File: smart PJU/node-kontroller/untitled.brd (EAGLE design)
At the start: 80 x 80 mm, 48 parts, among them J1 U.FL-R-SMT(01), J2 10118193-0001LF, K1 351, Q1 S9013, Q16 MMBT3904, Q17 MMBT3904, Q18 12MHz, U1 AMS1117, U19 CH340G, U2 PC817X2NIP0F

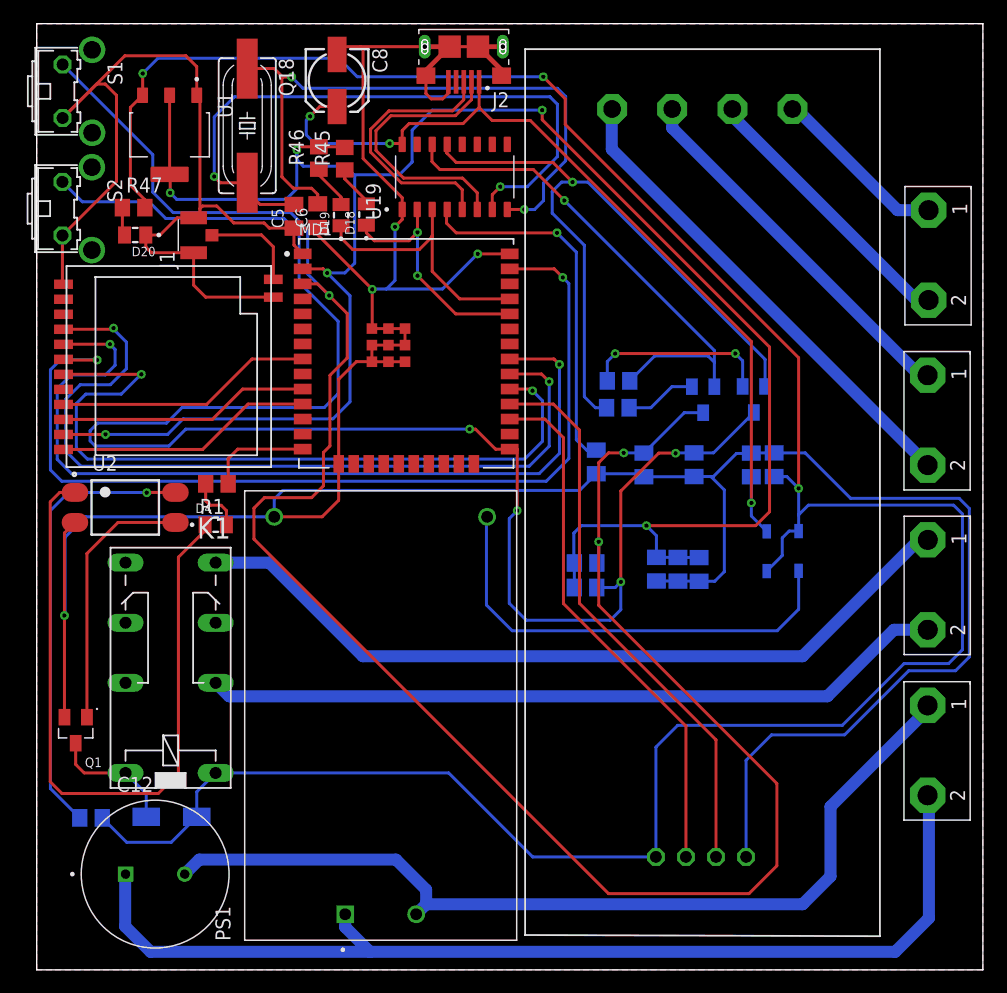
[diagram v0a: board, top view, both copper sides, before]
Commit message: revisi relay node dan list komponen
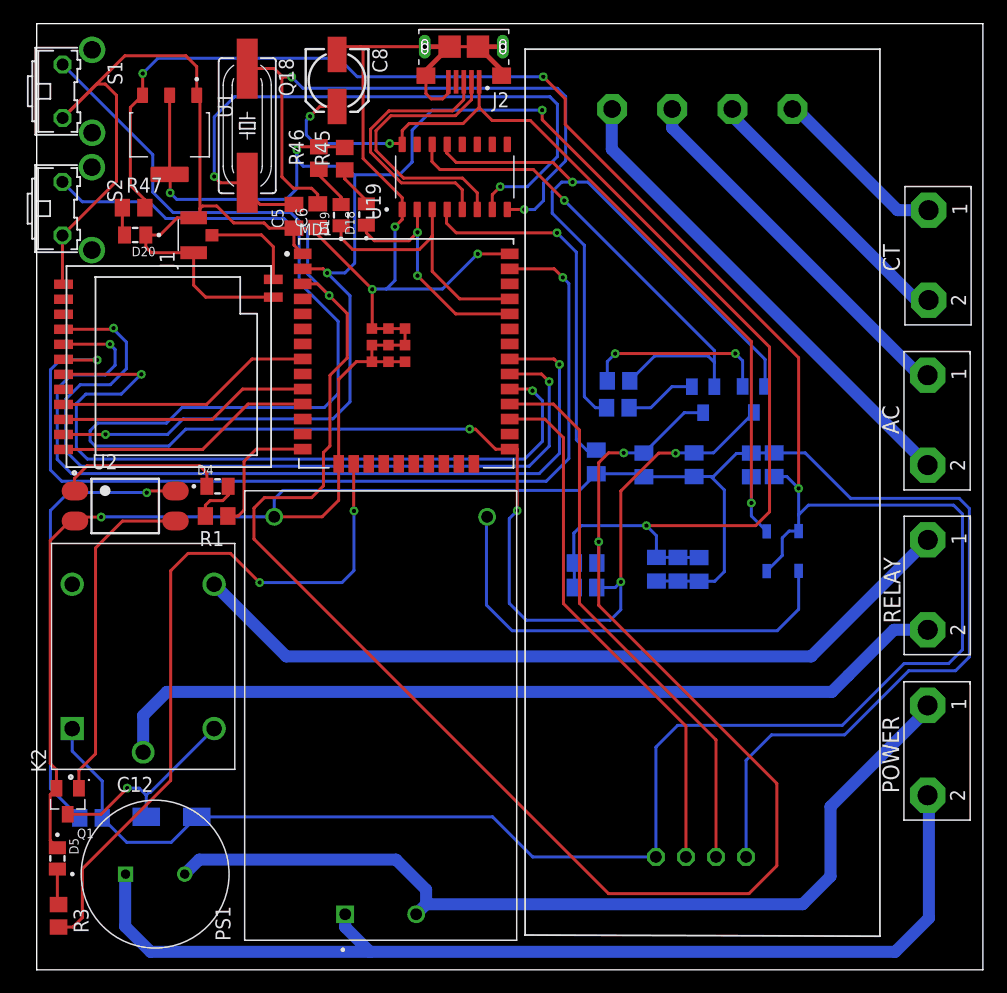
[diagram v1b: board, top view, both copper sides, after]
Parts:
- removed K1: 351, relay:351
- added D5: SML-LXT0805IW-TR, SML-LXT0805IW-TR:LEDC2012X120N
- added K2: SRD-05VDC-SL-C, SRD-05VDC-SL-C:RELAY_SRD-05VDC-SL-C
- added R3: 10k, rcl:R0805
- moved Q1 6.05 mm to (2.62, 14.3)
- moved D4 3.25 mm to (15.3, 40.9)
- moved R1 2.72 mm to (15.2, 38.4)
- moved U2 0.12 mm to (7.49, 39.2)
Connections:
- new net LED-LORA: MD1.16, R3.2
- new net N$12: D5.A, R3.1
- net GND: now also D5.C
- net N$10: now also K2.NO; no longer K1.S1
- net N$7: now also K2.A2; no longer K1.16
- net N$9: now also K2.COM; no longer K1.P1
- net VCC: now also K2.A1; no longer K1.1
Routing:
- net LED-LORA: track 0.00 -> 61.3 mm, vias 0 -> 2
- net N$4: track 60.0 -> 14.1 mm
- net N$9: track 63.0 -> 72.4 mm
- net N$7: track 10.8 -> 17.7 mm, vias 0 -> 1
- net N$6: track 22.4 -> 28.6 mm
- net GND: track 350.9 -> 355.4 mm
- net VCC: track 221.0 -> 225.3 mm
- net N$12: track 0.00 -> 3.04 mm
- net RELAY: track 8.77 -> 11.1 mm
- net N$8: track 4.72 -> 3.94 mm
- net N$10: track 67.6 -> 66.9 mm
- removed copper zone on layer 16, net N$12
- removed copper zone on layer 1, net N$13
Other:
- board text added: "AC"
- board text added: "CT"
- board text added: "POWER"
- board text added: "RELAY"

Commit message: revisi rangkaian
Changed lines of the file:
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@@
 <setting verticaltext="up"/>
 </settings>
-<grid distance="0.003125" unitdist="mic" unit="mm" style="lines" multiple="1" display="yes" altdistance="5" altunitdist="mil" altunit="mil"/>
+<grid distance="0.5" unitdist="mm" unit="mm" style="lines" multiple="1" display="yes" altdistance="5" altunitdist="mil" altunit="mil"/>
 <layers>
 <layer number="1" name="Top" color="4" fill="1" visible="yes" active="yes"/>
@@
 <wire x1="73.338565625" y1="25.897153125" x2="77.102621875" y2="25.897153125" width="0.254" layer="16"/>
 <wire x1="77.102621875" y1="25.897153125" x2="78.27220625" y2="27.0667375" width="0.254" layer="16"/>
-<wire x1="78.27220625" y1="27.0667375" x2="78.27220625" y2="38.539134375" width="0.254" layer="16"/>
-<wire x1="78.27220625" y1="38.539134375" x2="77.521609375" y2="39.28973125" width="0.254" layer="16"/>
-<wire x1="77.521609375" y1="39.28973125" x2="65.242903125" y2="39.28973125" width="0.254" layer="16"/>
-<wire x1="65.242903125" y1="39.28973125" x2="64.421646875" y2="38.468475" width="0.254" layer="16"/>
+<wire x1="78.27220625" y1="27.0667375" x2="78.27220625" y2="38.0002375" width="0.254" layer="16"/>
+<wire x1="78.27220625" y1="38.0002375" x2="77.113796875" y2="39.158646875" width="0.254" layer="16"/>
+<wire x1="77.113796875" y1="39.158646875" x2="65.11181875" y2="39.158646875" width="0.254" layer="16"/>
+<wire x1="65.11181875" y1="39.158646875" x2="64.421646875" y2="38.468475" width="0.254" layer="16"/>
 <wire x1="5.541034375" y1="12.848734375" x2="7.60865625" y2="10.7811125" width="0.254" layer="16"/>
 <wire x1="11.3760625" y1="10.7811125" x2="13.53185625" y2="12.93690625" width="0.254" layer="16"/>
@@
 <wire x1="77.686790625" y1="25.287809375" x2="78.857" y2="26.45801875" width="0.254" layer="16"/>
 <wire x1="78.857" y1="26.45801875" x2="78.857" y2="39.002490625" width="0.254" layer="16"/>
-<wire x1="78.857" y1="39.002490625" x2="77.99658125" y2="39.862909375" width="0.254" layer="16"/>
-<wire x1="77.99658125" y1="39.862909375" x2="68.821690625" y2="39.862909375" width="0.254" layer="16"/>
+<wire x1="78.857" y1="39.002490625" x2="77.83636875" y2="40.023121875" width="0.254" layer="16"/>
+<wire x1="77.83636875" y1="40.023121875" x2="68.661478125" y2="40.023121875" width="0.254" layer="16"/>
 <wire x1="64.979278125" y1="43.705321875" x2="62.35489375" y2="43.705321875" width="0.254" layer="16"/>
-<wire x1="68.821690625" y1="39.862909375" x2="64.979278125" y2="43.705321875" width="0.254" layer="16"/>
+<wire x1="68.661478125" y1="40.023121875" x2="64.979278125" y2="43.705321875" width="0.254" layer="16"/>
 <wire x1="55.583725" y1="41.70909375" x2="57.004628125" y2="41.70909375" width="0.254" layer="16"/>
 <wire x1="57.004628125" y1="41.70909375" x2="57.212775" y2="41.70909375" width="0.254" layer="16"/>
@@
 <wire x1="21.750346875" y1="62.711228125" x2="19.664753125" y2="62.711228125" width="0.254" layer="1"/>
 <wire x1="19.664753125" y1="62.711228125" x2="19.22711875" y2="63.1488625" width="0.254" layer="1"/>
-<wire x1="19.22711875" y1="63.1488625" x2="16.6598375" y2="63.1488625" width="0.254" layer="1"/>
-<wire x1="16.6598375" y1="63.1488625" x2="15.226446875" y2="64.582253125" width="0.254" layer="1"/>
+<wire x1="19.22711875" y1="63.1488625" x2="16.441365625" y2="63.1488625" width="0.254" layer="1"/>
+<wire x1="16.441365625" y1="63.1488625" x2="15.007975" y2="64.582253125" width="0.254" layer="1"/>
 <wire x1="13.529525" y1="73.9466875" x2="13.529525" y2="76.3655125" width="0.254" layer="1"/>
 <wire x1="13.529525" y1="76.3655125" x2="12.609725" y2="77.2853125" width="0.254" layer="1"/>
@@
 <wire x1="34.9094125" y1="78.05365" x2="37.3191875" y2="78.05365" width="0.254" layer="1"/>
 <wire x1="14.02280625" y1="64.582253125" x2="13.80331875" y2="64.362765625" width="0.254" layer="1"/>
-<wire x1="15.226446875" y1="64.582253125" x2="14.02280625" y2="64.582253125" width="0.254" layer="1"/>
+<wire x1="15.007975" y1="64.582253125" x2="14.02280625" y2="64.582253125" width="0.254" layer="1"/>
 <wire x1="1.669653125" y1="15.352003125" x2="1.669653125" y2="16.917603125" width="0.254" layer="1"/>
 <wire x1="1.669653125" y1="16.917603125" x2="1.143" y2="17.44425625" width="0.254" layer="1"/>
@@
 <wire x1="3.06565625" y1="3.61890625" x2="3.859878125" y2="4.413128125" width="0.254" layer="1"/>
 <wire x1="3.859878125" y1="4.413128125" x2="3.859878125" y2="8.543721875" width="0.254" layer="1"/>
-<wire x1="3.859878125" y1="8.543721875" x2="11.327715625" y2="16.011559375" width="0.254" layer="1"/>
-<wire x1="11.327715625" y1="16.011559375" x2="11.327715625" y2="33.740859375" width="0.254" layer="1"/>
-<wire x1="11.327715625" y1="33.740859375" x2="12.796546875" y2="35.209690625" width="0.254" layer="1"/>
-<wire x1="12.796546875" y1="35.209690625" x2="16.384671875" y2="35.209690625" width="0.254" layer="1"/>
+<wire x1="3.859878125" y1="8.543721875" x2="12.133284375" y2="16.817128125" width="0.254" layer="1"/>
+<wire x1="12.133284375" y1="16.817128125" x2="12.133284375" y2="33.980696875" width="0.254" layer="1"/>
+<wire x1="12.133284375" y1="33.980696875" x2="13.362278125" y2="35.209690625" width="0.254" layer="1"/>
+<wire x1="13.362278125" y1="35.209690625" x2="16.384671875" y2="35.209690625" width="0.254" layer="1"/>
 <wire x1="16.384671875" y1="35.209690625" x2="18.8504375" y2="32.743925" width="0.254" layer="1"/>
 <via x="18.8504375" y="32.743925" extent="1-16" drill="0.35"/>
